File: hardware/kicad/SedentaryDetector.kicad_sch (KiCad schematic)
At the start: 3 parts, among them J1 ESP32_2x15, J2 MPU6050_1x8, J3 POWER_2P

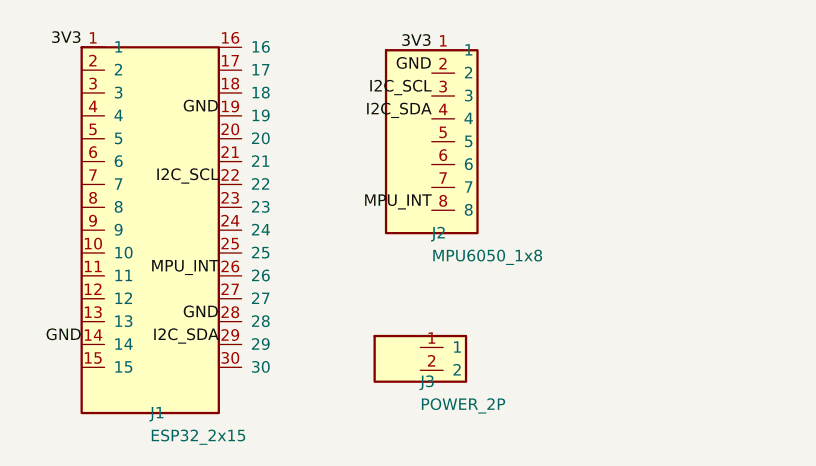
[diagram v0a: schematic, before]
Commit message: docs/hardware: 正式选型 GY-87 并修正 J2 引脚顺序
联调验证 MPU6050 后统一文档与 KiCad 原理图 v0.5.1（背面照片导致 Pin1–8 反转）；补充固件源码与 GY-87 实物图。

Co-authored-by: Cursor <cursoragent@cursor.com>
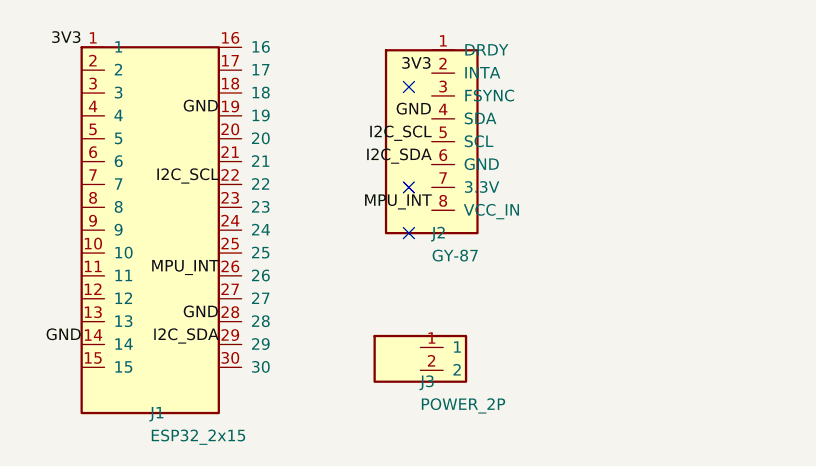
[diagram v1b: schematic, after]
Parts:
- J2: value MPU6050_1x8 -> GY-87
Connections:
- net 3V3: now also J2.2 (INTA); no longer J2.1
- net GND: now also J2.4 (SDA); no longer J2.2
- net I2C_SCL: now also J2.5 (SCL); no longer J2.3
- net I2C_SDA: now also J2.6 (GND); no longer J2.4
- no-connect marks 0 -> 3
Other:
- moved on the sheet: J2
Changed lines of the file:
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@@
 	(title_block
 		(title "Sedentary Detector")
-		(date "2026-06-20")
-		(rev "0.2")
+		(date "2026-06-22")
+		(rev "0.5.1")
+		(comment 1 "J2 GY-87 Pin1=DRDY..Pin8=VCC_IN (载板正面插入; 模块背照丝印顺序相反)")
 	)
 	(label "3V3"
@@
 	)
 	(label "GND"
-		(at 81.28 82.55 180)
+		(at 81.28 87.63 180)
 		(effects
 			(font
@@
 	)
 	(label "I2C_SCL"
-		(at 81.28 85.09 180)
+		(at 81.28 90.17 180)
 		(effects
 			(font
@@
 	)
 	(label "I2C_SDA"
-		(at 81.28 87.63 180)
+		(at 81.28 92.71 180)
 		(effects
 			(font
@@
 	)
 	(label "3V3"
-		(at 81.28 80.01 180)
+		(at 81.28 82.55 180)
 		(effects
 			(font
@@
 			(justify right bottom)
 		)
+	)
+	(no_connect
+		(at 78.74 100.33)
+	)
+	(no_connect
+		(at 78.74 95.25)
+	)
+	(no_connect
+		(at 78.74 84.09)
 	)
 	(symbol
@@
 			)
 		)
-		(property "Value" "MPU6050_1x8"
+		(property "Value" "GY-87"
 			(at 81.28 102.87 0)
 			(show_name no)

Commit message: hardware: 载板简化为 MCU/IMU/OLED/电源 v0.6
移除载板滑动开关与 CAL/OK 按键；更新 KiCad 原理图/PCB、文档与固件配套改动。

Co-authored-by: Cursor <cursoragent@cursor.com>
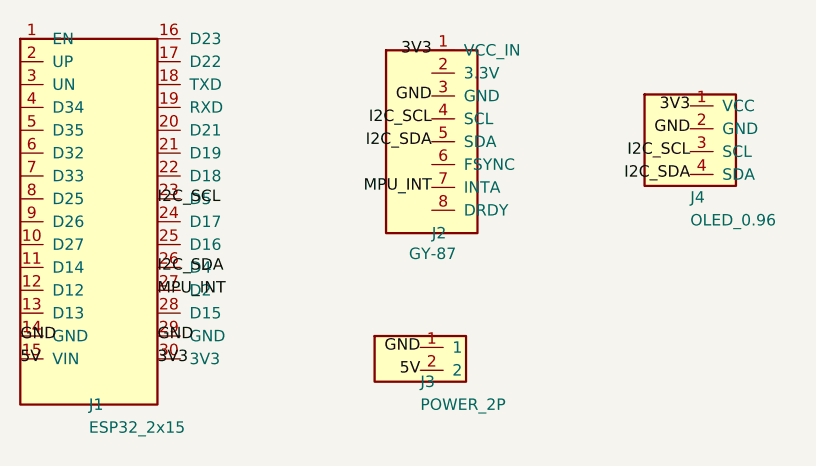
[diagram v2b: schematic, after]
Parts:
- added J4: OLED_0.96, symbol Conn_01x04
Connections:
- net 3V3: now also J1.30 (3V3), J2.1 (VCC_IN), J4.1 (VCC); no longer J1.1, J2.2 (INTA)
- net GND: now also J1.29 (GND), J2.3 (GND), J3.1, J4.2 (GND); no longer J1.19, J1.28, J2.4 (SDA)
- net I2C_SCL: now also J1.23 (D5), J2.4 (SCL), J4.3 (SCL); no longer J1.22, J2.5 (SCL)
- net I2C_SDA: now also J1.26 (D4), J2.5 (SDA), J4.4 (SDA); no longer J1.29, J2.6 (GND)
- net MPU_INT: now also J1.27 (D2), J2.7 (INTA); no longer J1.26, J2.8 (VCC_IN)
- net 5V: now reaches J3.2
- net 5V: now also J1.15 (VIN)
- no-connect marks 3 -> 0
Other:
- moved on the sheet: J1
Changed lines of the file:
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@@
 		(title "Sedentary Detector")
 		(date "2026-06-22")
-		(rev "0.5.1")
-		(comment 1 "J2 GY-87 Pin1=DRDY..Pin8=VCC_IN (载板正面插入; 模块背照丝印顺序相反)")
+		(rev "0.6")
+		(comment 1 "MCU+GY-87+OLED+PM11 only; no carrier switches/buttons")
 	)
 	(label "3V3"
-		(at 42.38 79.68 180)
-		(effects
-			(font
-				(size 1.27 1.27)
-			)
-			(justify right bottom)
+		(at 50.8 114.3 0)
+		(effects
+			(font
+				(size 1.27 1.27)
+			)
+			(justify left)
+		)
+	)
+	(label "GND"
+		(at 50.8 111.76 0)
+		(effects
+			(font
+				(size 1.27 1.27)
+			)
+			(justify left)
+		)
+	)
+	(label "I2C_SCL"
+		(at 50.8 96.52 0)
+		(effects
+			(font
+				(size 1.27 1.27)
+			)
+			(justify left)
+		)
+	)
+	(label "I2C_SDA"
+		(at 50.8 104.14 0)
+		(effects
+			(font
+				(size 1.27 1.27)
+			)
+			(justify left)
 		)
 	)
 	(label "MPU_INT"
-		(at 57.62 105.08 180)
-		(effects
-			(font
-				(size 1.27 1.27)
-			)
-			(justify right bottom)
+		(at 50.8 106.68 0)
+		(effects
+			(font
+				(size 1.27 1.27)
+			)
+			(justify left)
+		)
+	)
+	(label "3V3"
+		(at 81.28 80.01 180)
+		(effects
+			(font
+				(size 1.27 1.27)
+			)
+			(justify right)
 		)
 	)
 	(label "GND"
+		(at 81.28 85.09 180)
+		(effects
+			(font
+				(size 1.27 1.27)
+			)
+			(justify right)
+		)
+	)
+	(label "I2C_SCL"
 		(at 81.28 87.63 180)
 		(effects
@@
 				(size 1.27 1.27)
 			)
-			(justify right bottom)
-		)
-	)
-	(label "I2C_SCL"
+			(justify right)
+		)
+	)
+	(label "I2C_SDA"
 		(at 81.28 90.17 180)
 		(effects
@@
 				(size 1.27 1.27)
 			)
-			(justify right bottom)
-		)
-	)
-	(label "I2C_SDA"
-		(at 81.28 92.71 180)
-		(effects
-			(font
-				(size 1.27 1.27)
-			)
-			(justify right bottom)
-		)
-	)
-	(label "I2C_SDA"
-		(at 57.62 112.7 180)
-		(effects
-			(font
-				(size 1.27 1.27)
-			)
-			(justify right bottom)
-		)
-	)
-	(label "3V3"
-		(at 81.28 82.55 180)
-		(effects
-			(font
-				(size 1.27 1.27)
-			)
-			(justify right bottom)
+			(justify right)
+		)
+	)
+	(label "MPU_INT"
+		(at 81.28 95.25 180)
+		(effects
+			(font
+				(size 1.27 1.27)
+			)
+			(justify right)
 		)
 	)
 	(label "GND"
-		(at 57.62 87.3 180)
-		(effects
-			(font
-				(size 1.27 1.27)
-			)
-			(justify right bottom)
-		)
-	)
-	(label "MPU_INT"
-		(at 81.28 97.79 180)
-		(effects
-			(font
-				(size 1.27 1.27)
-			)
-			(justify right bottom)
-		)
-	)
-	(label "GND"
-		(at 57.62 110.16 180)
-		(effects
-			(font
-				(size 1.27 1.27)
-			)
-			(justify right bottom)
-		)
-	)
-	(label "GND"
-		(at 42.38 112.7 180)
-		(effects
-			(font
-				(size 1.27 1.27)
-			)
-			(justify right bottom)
-		)
-	)
-	(label "I2C_SCL"
-		(at 57.62 94.92 180)
-		(effects
-			(font
-				(size 1.27 1.27)
-			)
-			(justify right bottom)
-		)
-	)
-	(no_connect
-		(at 78.74 100.33)
-	)
-	(no_connect
-		(at 78.74 95.25)
-	)
-	(no_connect
-		(at 78.74 84.09)
+		(at 35.56 111.76 0)
+		(effects
+			(font
+				(size 1.27 1.27)
+			)
+			(justify left)
+		)
+	)
+	(label "5V" (at 35.56 114.30 0)
+		(effects (font (size 1.27 1.27)) (justify left))
+	)
+	(label "GND" (at 80.01 113.03 180)
+		(effects (font (size 1.27 1.27)) (justify right))
+	)
+	(label "5V" (at 80.01 115.57 180)
+		(effects (font (size 1.27 1.27)) (justify right))
 	)
 	(symbol
@@
 		)
 		(property "Value" "GY-87"
-			(at 81.28 102.87 0)
+			(at 78.74 102.616 0)
 			(show_name no)
 			(do_not_autoplace no)
@@
 	(symbol
 		(lib_id "Conn_02x15")
-		(at 50 100 0)
+		(at 43.18 99.06 0)
 		(unit 1)
 		(body_style 1)
@@
 		(dnp no)
 		(property "Reference" "J1"
-			(at 50 120.32 0)
+			(at 43.18 119.38 0)
 			(show_name no)
 			(do_not_autoplace no)
@@
 		)
 		(property "Value" "ESP32_2x15"
-			(at 50 122.86 0)
+			(at 43.18 121.92 0)
 			(show_name no)
 			(do_not_autoplace no)
@@
 		)
 		(property "Footprint" ""
-			(at 50 80 0)
+			(at 43.18 79.06 0)
 			(hide yes)
 			(show_name no)
@@
 		)
 		(property "Datasheet" ""
-			(at 50 80 0)
+			(at 43.18 79.06 0)
 			(hide yes)
 			(show_name no)
@@
 		)
 		(property "Description" ""
-			(at 50 100 0)
+			(at 43.18 99.06 0)
 			(show_name no)
 			(do_not_autoplace no)
@@
 		)
 	)
+	(label "3V3" (at 110 86.19 180) (effects (font (size 1.27 1.27)) (justify right))
+)
+	(label "GND" (at 110 88.73 180) (effects (font (size 1.27 1.27)) (justify right))
+)
+	(label "I2C_SCL" (at 110 91.27 180) (effects (font (size 1.27 1.27)) (justify right))
+)
+	(label "I2C_SDA" (at 110 93.81 180) (effects (font (size 1.27 1.27)) (justify right))
+)
+	(symbol
+		(lib_id "Conn_01x04")
+		(at 110 90 0)
+		(unit 1) (body_style 1)
+		(exclude_from_sim no) (in_bom yes) (on_board yes) (in_pos_files yes) (dnp no)
+		(property "Reference" "J4" (at 110 96.35 0) (show_name no) (do_not_autoplace no)
+			(effects (font (size 1.27 1.27)) (justify left)))
+		(property "Value" "OLED_0.96" (at 110 98.89 0) (show_name no) (do_not_autoplace no)
+			(effects (font (size 1.27 1.27)) (justify left)))
+		(property "Footprint" "" (at 110 83.65 0) (hide yes) (show_name no) (do_not_autoplace no)
+			(effects (font (size 1.27 1.27))))
+		(property "Datasheet" "" (at 110 90 0) (hide yes) (show_name no) (do_not_autoplace no)
+			(effects (font (size 1.27 1.27))))
+		(property "Description" "" (at 110 90 0) (hide yes) (show_name no) (do_not_autoplace no)
+			(effects (font (size 1.27 1.27))))
+		(pin "1")
+		(pin "2")
+		(pin "3")
+		(pin "4")
+		(instances
+			(project "SedentaryDetector"
+				(path "/c9bb8533-5510-495a-86a1-47335bb4bfe4"
+					(reference "J4") (unit 1))))
+	)
 	(sheet_instances
